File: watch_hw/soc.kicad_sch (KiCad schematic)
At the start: 28 parts, among them U1 NRF52833-QDAA, Y1 32MHz, Y2 32.768kHz

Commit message: Routing progress
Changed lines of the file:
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@@
     (effects (font (size 1.27 1.27)) (justify left bottom))
   )
-  (hierarchical_label "HR_INT" (shape input) (at 261.62 124.46 0) (fields_autoplaced)
+  (hierarchical_label "HR_INT" (shape input) (at 261.62 121.92 0) (fields_autoplaced)
     (effects (font (size 1.27 1.27)) (justify left))
   )
-  (hierarchical_label "DISP_SCLK" (shape output) (at 261.62 111.76 0) (fields_autoplaced)
+  (hierarchical_label "DISP_CS" (shape output) (at 261.62 111.76 0) (fields_autoplaced)
     (effects (font (size 1.27 1.27)) (justify left))
   )
-  (hierarchical_label "DISP_INVERT" (shape output) (at 261.62 116.84 0) (fields_autoplaced)
+  (hierarchical_label "DISP_SCLK" (shape output) (at 261.62 114.3 0) (fields_autoplaced)
     (effects (font (size 1.27 1.27)) (justify left))
   )
-  (hierarchical_label "ACC_INT1" (shape input) (at 261.62 132.08 0) (fields_autoplaced)
+  (hierarchical_label "ACC_INT1" (shape input) (at 261.62 124.46 0) (fields_autoplaced)
     (effects (font (size 1.27 1.27)) (justify left))
   )
-  (hierarchical_label "BTN1" (shape input) (at 261.62 144.78 0) (fields_autoplaced)
+  (hierarchical_label "BTN1" (shape input) (at 261.62 137.16 0) (fields_autoplaced)
     (effects (font (size 1.27 1.27)) (justify left))
   )
@@
     (effects (font (size 1.27 1.27)) (justify left))
   )
-  (hierarchical_label "DISP_SDO" (shape output) (at 261.62 114.3 0) (fields_autoplaced)
+  (hierarchical_label "DISP_SDO" (shape output) (at 261.62 116.84 0) (fields_autoplaced)
     (effects (font (size 1.27 1.27)) (justify left))
   )
-  (hierarchical_label "MOTOR_EN" (shape output) (at 261.62 149.86 0) (fields_autoplaced)
+  (hierarchical_label "MOTOR_EN" (shape output) (at 261.62 142.24 0) (fields_autoplaced)
     (effects (font (size 1.27 1.27)) (justify left))
   )
-  (hierarchical_label "ACC_INT2" (shape input) (at 261.62 134.62 0) (fields_autoplaced)
+  (hierarchical_label "ACC_INT2" (shape input) (at 261.62 127 0) (fields_autoplaced)
     (effects (font (size 1.27 1.27)) (justify left))
   )
-  (hierarchical_label "BACKLIGHT" (shape output) (at 261.62 121.92 0) (fields_autoplaced)
+  (hierarchical_label "BACKLIGHT" (shape output) (at 261.62 119.38 0) (fields_autoplaced)
     (effects (font (size 1.27 1.27)) (justify left))
   )
@@
     (effects (font (size 1.27 1.27)) (justify left))
   )
-  (hierarchical_label "HR_GPIO" (shape bidirectional) (at 261.62 127 0) (fields_autoplaced)
-    (effects (font (size 1.27 1.27)) (justify left))
-  )
-  (hierarchical_label "DISP_ON" (shape output) (at 261.62 119.38 0) (fields_autoplaced)
-    (effects (font (size 1.27 1.27)) (justify left))
-  )
-  (hierarchical_label "SDA" (shape bidirectional) (at 261.62 139.7 0) (fields_autoplaced)
+  (hierarchical_label "SDA" (shape bidirectional) (at 261.62 132.08 0) (fields_autoplaced)
     (effects (font (size 1.27 1.27)) (justify left))
   )
@@
     (effects (font (size 1.27 1.27)) (justify left))
   )
-  (hierarchical_label "MOTOR" (shape output) (at 261.62 147.32 0) (fields_autoplaced)
+  (hierarchical_label "MOTOR" (shape output) (at 261.62 139.7 0) (fields_autoplaced)
     (effects (font (size 1.27 1.27)) (justify left))
   )
-  (hierarchical_label "HR_LDO_EN" (shape output) (at 261.62 129.54 0) (fields_autoplaced)
+  (hierarchical_label "SCL" (shape output) (at 261.62 129.54 0) (fields_autoplaced)
     (effects (font (size 1.27 1.27)) (justify left))
   )
-  (hierarchical_label "SCL" (shape output) (at 261.62 137.16 0) (fields_autoplaced)
+  (hierarchical_label "BTN0" (shape input) (at 261.62 134.62 0) (fields_autoplaced)
     (effects (font (size 1.27 1.27)) (justify left))
   )
-  (hierarchical_label "BTN0" (shape input) (at 261.62 142.24 0) (fields_autoplaced)
-    (effects (font (size 1.27 1.27)) (justify left))
-  )

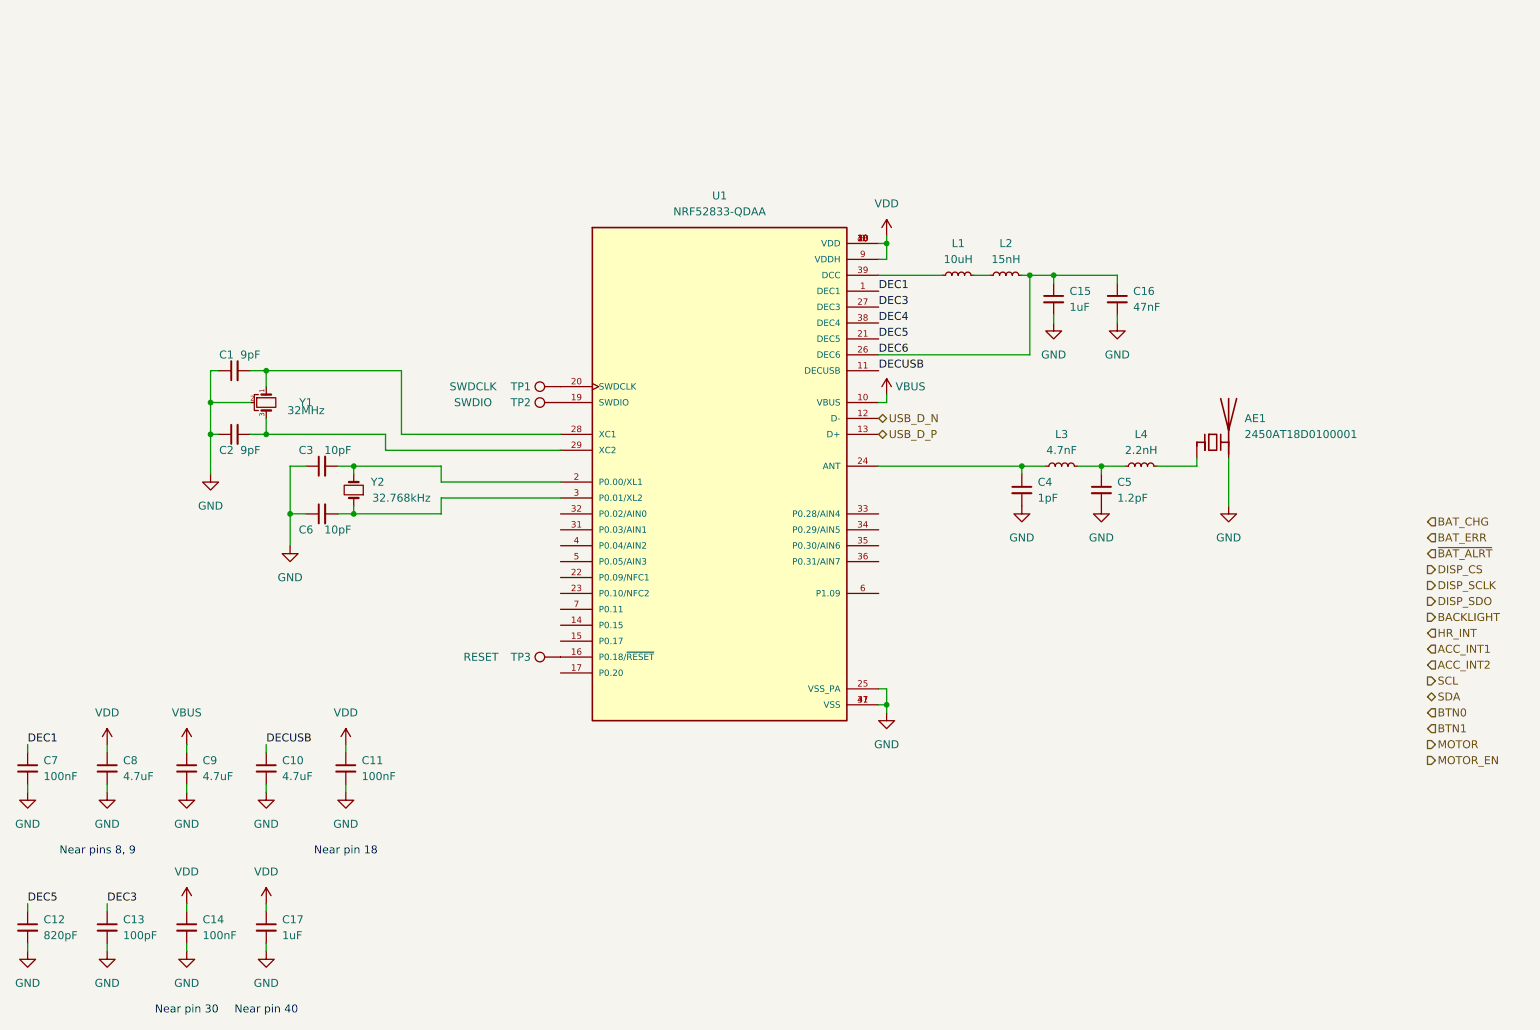
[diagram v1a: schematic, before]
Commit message: Clean up library symbols, update to kicad 8
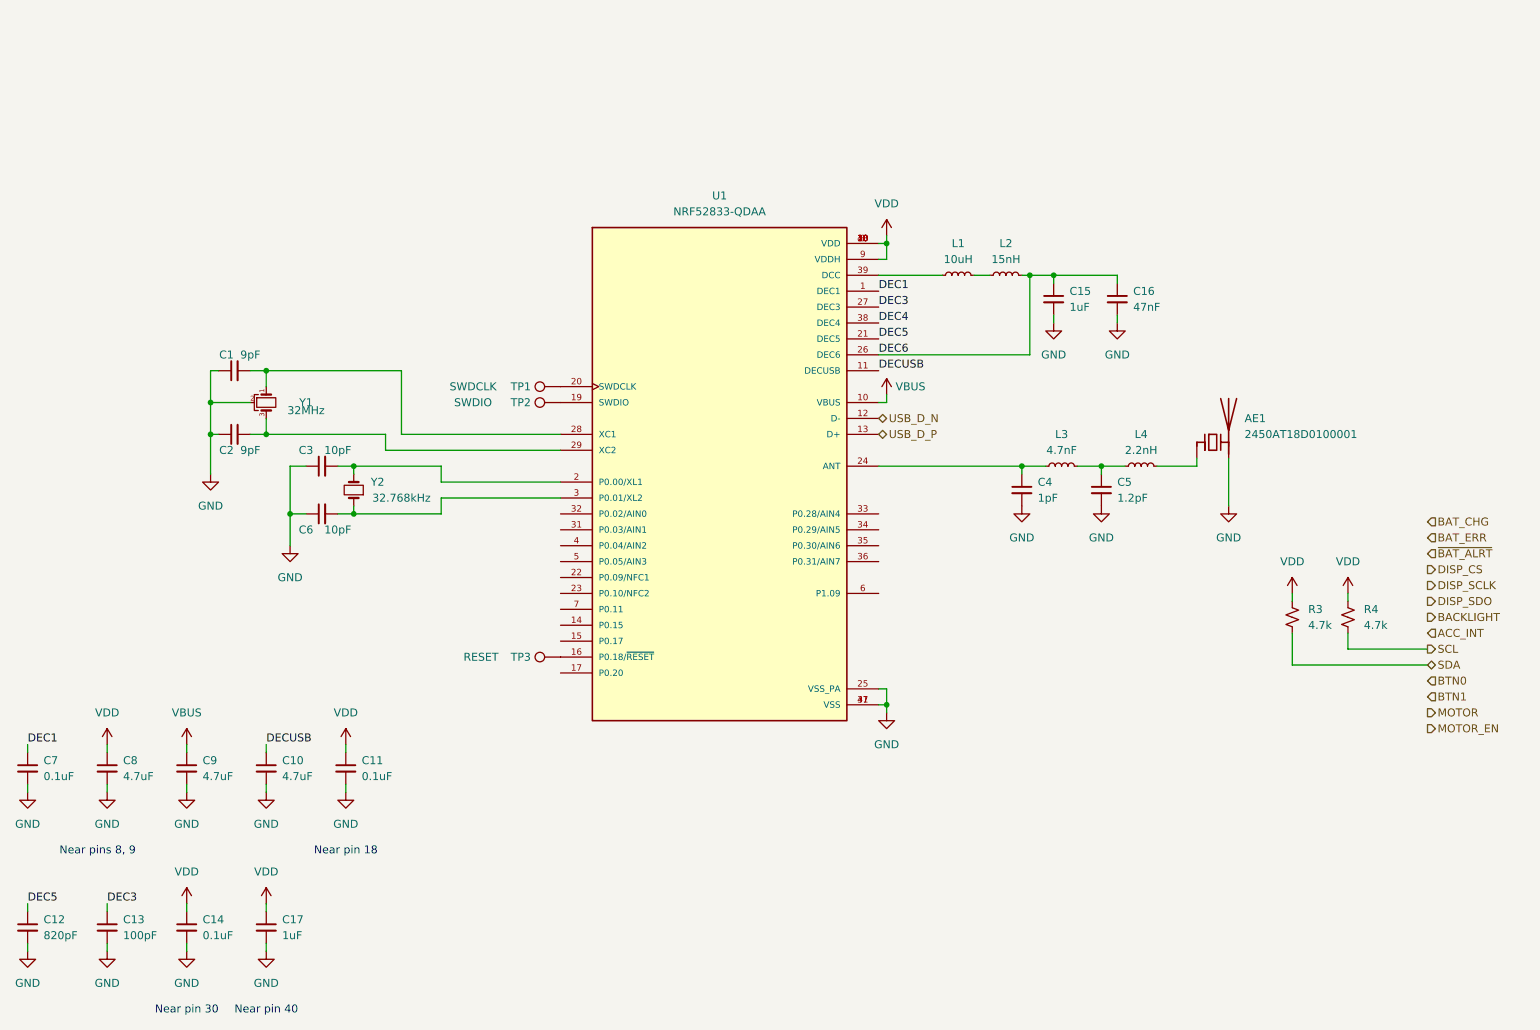
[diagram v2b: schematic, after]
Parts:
- added R3, R4: 4.7k, Resistor_SMD:R_0402_1005Metric_Pad0.72x0.64mm_HandSolder, symbol Device:R_Small_US
- C11, C14, C7: value 100nF -> 0.1uF
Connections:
- net SCL: now also R4.2
- net SDA: now also R3.2
- net VDD: now also R3.1, R4.1

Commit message: SCH: add STM32 and most passives
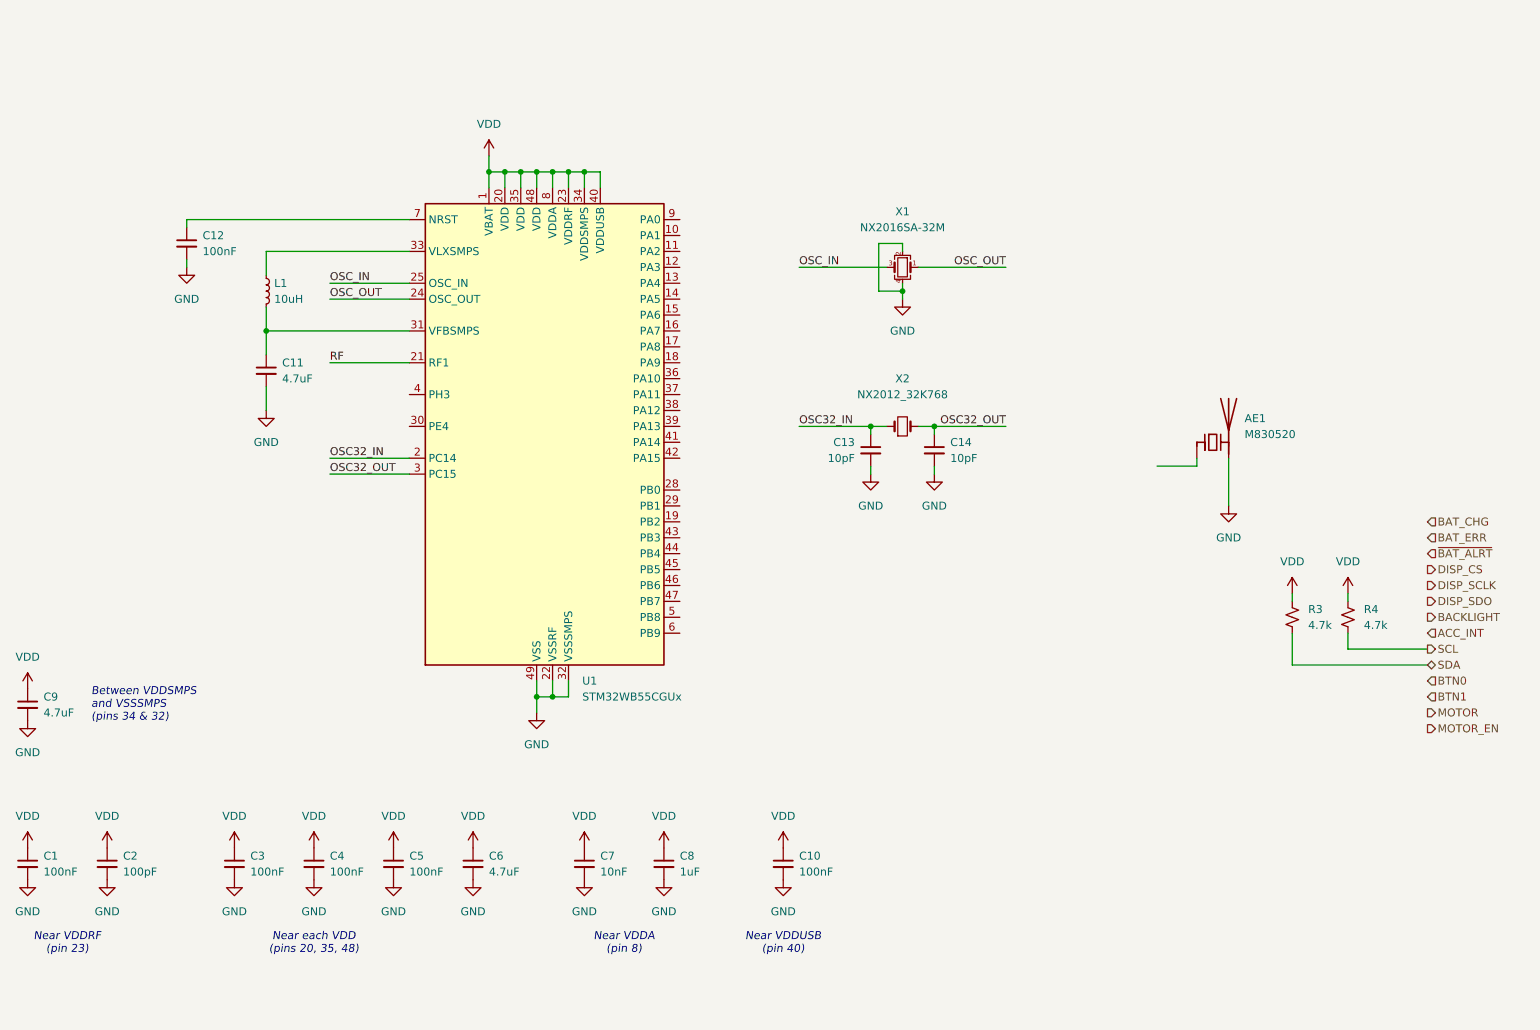
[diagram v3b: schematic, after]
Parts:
- removed C15, C17: 1uF, Capacitor_SMD:C_0402_1005Metric_Pad0.74x0.62mm_HandSolder, symbol Device:C_Small
- removed C16: 47nF, Capacitor_SMD:C_0402_1005Metric_Pad0.74x0.62mm_HandSolder, symbol Device:C_Small
- removed L2: 15nH, Inductor_SMD:L_0402_1005Metric_Pad0.77x0.64mm_HandSolder, symbol Device:L_Small
- removed L3: 4.7nF, Inductor_SMD:L_0402_1005Metric_Pad0.77x0.64mm_HandSolder, symbol Device:L_Small
- removed L4: 2.2nH, Inductor_SMD:L_0402_1005Metric_Pad0.77x0.64mm_HandSolder, symbol Device:L_Small
- removed TP1: SWDCLK, TestPoint:TestPoint_THTPad_D1.0mm_Drill0.5mm, symbol Connector:TestPoint
- removed TP2: SWDIO, TestPoint:TestPoint_THTPad_D1.0mm_Drill0.5mm, symbol Connector:TestPoint
- removed TP3: RESET, TestPoint:TestPoint_THTPad_D1.0mm_Drill0.5mm, symbol Connector:TestPoint
- removed U1: NRF52833-QDAA, watch:nRF52833-QD, symbol watch:NRF52833-QDAA-R7
- removed Y1: 32MHz, watch:XTAL_ECX-1637B2, symbol Device:Crystal_GND2_Small
- removed Y2: 32.768kHz, watch:XTAL_SC32S, symbol Device:Crystal_Small
- added U1: STM32WB55CGUx, Package_DFN_QFN:QFN-48-1EP_7x7mm_P0.5mm_EP3.5x3.5mm_ThermalVias, symbol MCU_ST_STM32WB:STM32WB55CGUx
- added X1: NX2016SA-32M, Crystal:Crystal_SMD_2016-4Pin_2.0x1.6mm, symbol Device:Crystal_GND24_Small
- added X2: NX2012_32K768, Crystal:Crystal_SMD_2012-2Pin_2.0x1.2mm_HandSoldering, symbol Device:Crystal_Small
- AE1: value 2450AT18D0100001 -> M830520; footprint watch:ANTENNA_2450AT18D0100001 -> (none); Manufacturer (none) -> Kyocera AVX
- C1: value 9pF -> 100nF
- C10: value 4.7uF -> 100nF
- C11: value 0.1uF -> 4.7uF
- C12: value 820pF -> 100nF
- C13: value 100pF -> 10pF
- C14: value 0.1uF -> 10pF
- C2: value 9pF -> 100pF
- C3: value 10pF -> 100nF
- C4: value 1pF -> 100nF
- C5: value 1.2pF -> 100nF
- C6: value 10pF -> 4.7uF
- C7: value 0.1uF -> 10nF
- C8: value 4.7uF -> 1uF
- L1: footprint Inductor_SMD:L_0805_2012Metric_Pad1.05x1.20mm_HandSolder -> Inductor_SMD:L_0805_2012Metric_Pad1.15x1.40mm_HandSolder; Manufacturer (none) -> Murata; Manufacturer Part Number (none) -> LQM21FN100M70L
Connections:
- net DEC1 is gone; now on net VDD: C7.1
- net DECUSB is gone; now on net VDD: C10.1
- net VBUS is gone; now on net VDD: C9.1
- net GND: now also C1.2, C2.2, C3.2, C6.2, U1.22 (VSSRF), U1.32 (VSSSMPS), U1.49 (VSS), X1.2, X1.4; no longer C1.1, C2.1, C3.1, C6.1
- net VDD: now also C1.1, C2.1, C3.1, C4.1, C5.1, C6.1, U1.1 (VBAT), U1.20 (VDD), U1.23 (VDDRF), U1.34 (VDDSMPS), U1.35 (VDD), U1.40 (VDDUSB), U1.48 (VDD), U1.8 (VDDA); no longer C11.1, C14.1
- net at L1.1: now also U1.33 (VLXSMPS)
- net at L1.2: now also C11.1, U1.31 (VFBSMPS)
- net DEC3 renamed OSC32_IN
- net OSC32_IN: now also U1.2 (PC14), X2.1
- net DEC5: no longer names the net of C12.1
- net DEC5: now also U1.7 (NRST)
- new net OSC32_OUT: C14.1, U1.3 (PC15), X2.2
- new net OSC_IN: U1.25 (OSC_IN), X1.3
- new net OSC_OUT: U1.24 (OSC_OUT), X1.1
- new net RF: U1.21 (RF1)
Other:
- note added: "Between VDDSMPS and VSSSMPS (pins 34 & 32)"
- note added: "Near VDDA (pin 8)"
- note added: "Near VDDRF (pin 23)"
- note added: "Near VDDUSB (pin 40)"
- note added: "Near each VDD (pins 20, 35, 48)"
- note removed: "Near pin 18"
- note removed: "Near pin 30"
- note removed: "Near pin 40"
- note removed: "Near pins 8, 9"

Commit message: Start watch v1 layout
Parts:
- removed AE1: M830520, symbol Device:Antenna_Chip
- added J3: Conn_ARM_SWD_TagConnect_TC2030-NL, Connector:Tag-Connect_TC2030-IDC-NL_2x03_P1.27mm_Vertical, symbol Connector:Conn_ARM_SWD_TagConnect_TC2030-NL
- U1: footprint Package_DFN_QFN:QFN-48-1EP_7x7mm_P0.5mm_EP3.5x3.5mm_ThermalVias -> Package_DFN_QFN:QFN-48-1EP_7x7mm_P0.5mm_EP3.5x3.5mm
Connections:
- net GND: now also J3.5 (GND)
- net VDD: now also J3.1 (VCC)
- net NRST: now reaches C12.1, U1.7 (NRST)
- net NRST: now also J3.3 (~{RESET})
- net SWDIO: now reaches U1.39 (PA13)
- net SWDIO: now also J3.2 (SWDIO)
- net SWCLK: now reaches U1.41 (PA14)
- net SWCLK: now also J3.4 (SWCLK)
- net RF: no longer names the net of U1.21 (RF1)
- no-connect marks 0 -> 2
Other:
- moved on the sheet: C13, C14, X1, X2

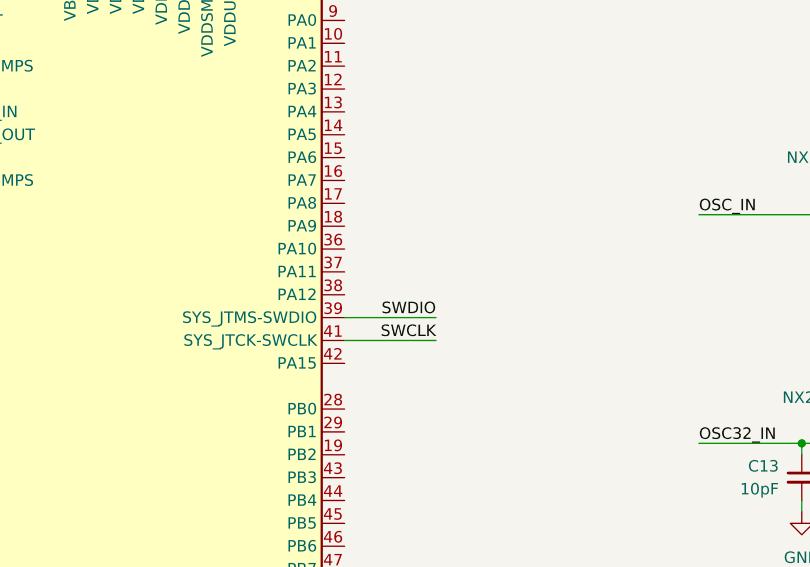
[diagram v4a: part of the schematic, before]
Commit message: Route usb data
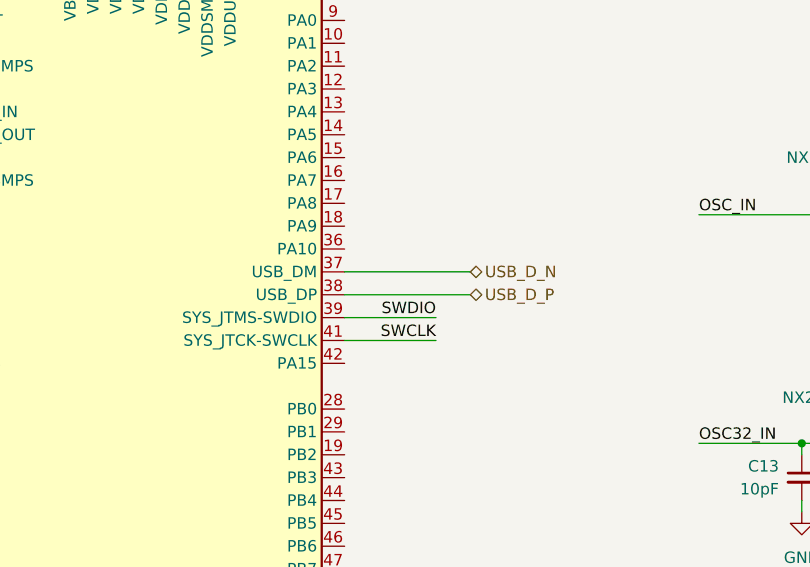
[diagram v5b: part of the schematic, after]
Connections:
- net USB_D_N: now reaches U1.37 (PA11)
- net USB_D_P: now reaches U1.38 (PA12)
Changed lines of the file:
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@@
 	(wire
 		(pts
+			(xy 144.78 83.82) (xy 158.75 83.82)
+		)
+		(stroke
+			(width 0)
+			(type default)
+		)
+	)
+	(wire
+		(pts
 			(xy 119.38 132.08) (xy 119.38 134.62)
 		)
@@
 	(wire
 		(pts
+			(xy 144.78 86.36) (xy 158.75 86.36)
+		)
+		(stroke
+			(width 0)
+			(type default)
+		)
+	)
+	(wire
+		(pts
 			(xy 200.66 73.66) (xy 196.85 73.66)
 		)
@@
 		)
 	)
+	(hierarchical_label "USB_D_N"
+		(shape bidirectional)
+		(at 158.75 83.82 0)
+		(effects
+			(font
+				(size 1.27 1.27)
+			)
+			(justify left)
+		)
+	)
 	(hierarchical_label "BTN1"
 		(shape input)
@@
 		)
 	)
+	(hierarchical_label "USB_D_P"
+		(shape bidirectional)
+		(at 158.75 86.36 0)
+		(effects
+			(font
+				(size 1.27 1.27)
+			)
+			(justify left)
+		)
+	)
 	(hierarchical_label "SCL"
 		(shape output)
@@
 		)
 		(pin "38"
+			(alternate "USB_DP")
 		)
 		(pin "49"
@@
 		)
 		(pin "37"
+			(alternate "USB_DM")
 		)
 		(pin "8"
